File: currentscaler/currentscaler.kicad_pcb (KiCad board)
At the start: 2 copper layers, 76.1 x 33.4 mm, 27 parts, among them CON1 RS677-8759, CON2 RS677-8759, U1 LMV321, U2 MAX4239AUT, U3 MAX4239AUT

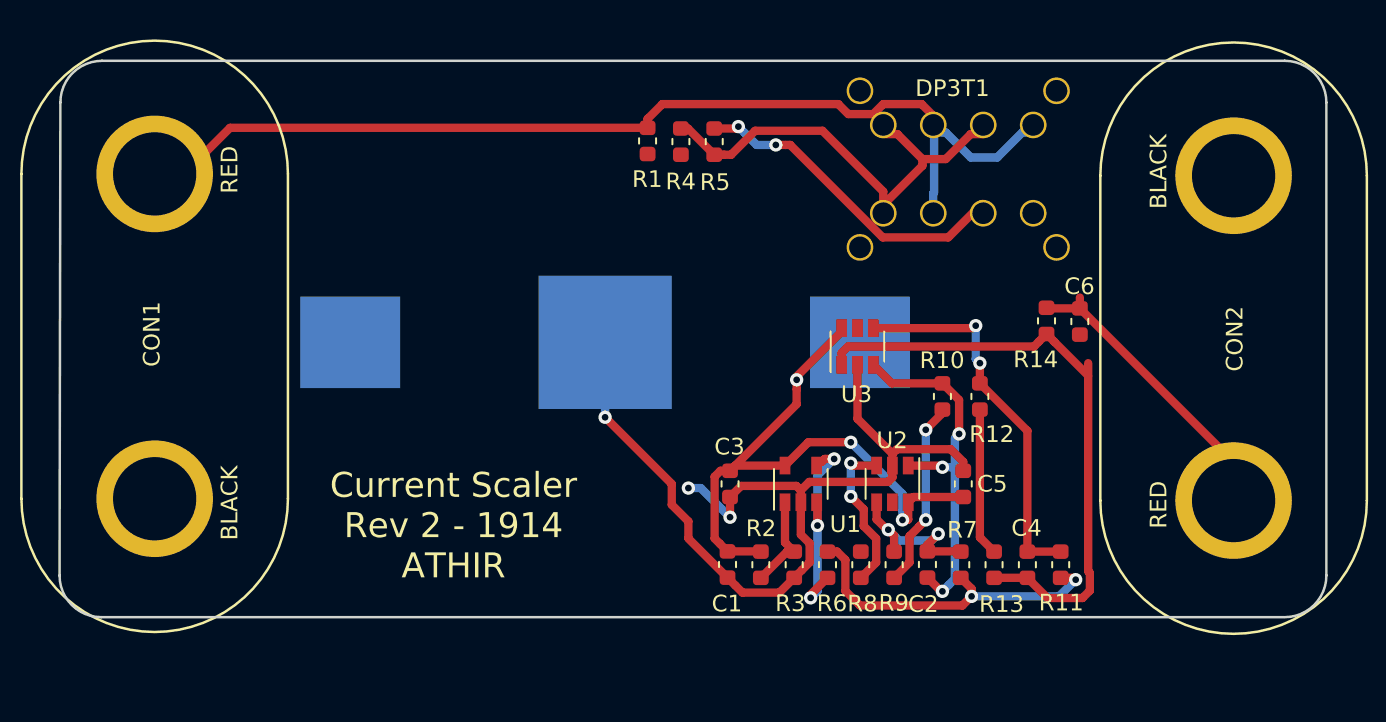
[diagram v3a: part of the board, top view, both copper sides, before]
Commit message: WIP: HW4
100 ohm resistors now 0805.
Fixed footprint of switch.
Removed 3V CR2450 holder.
Added silkscreen explanations.
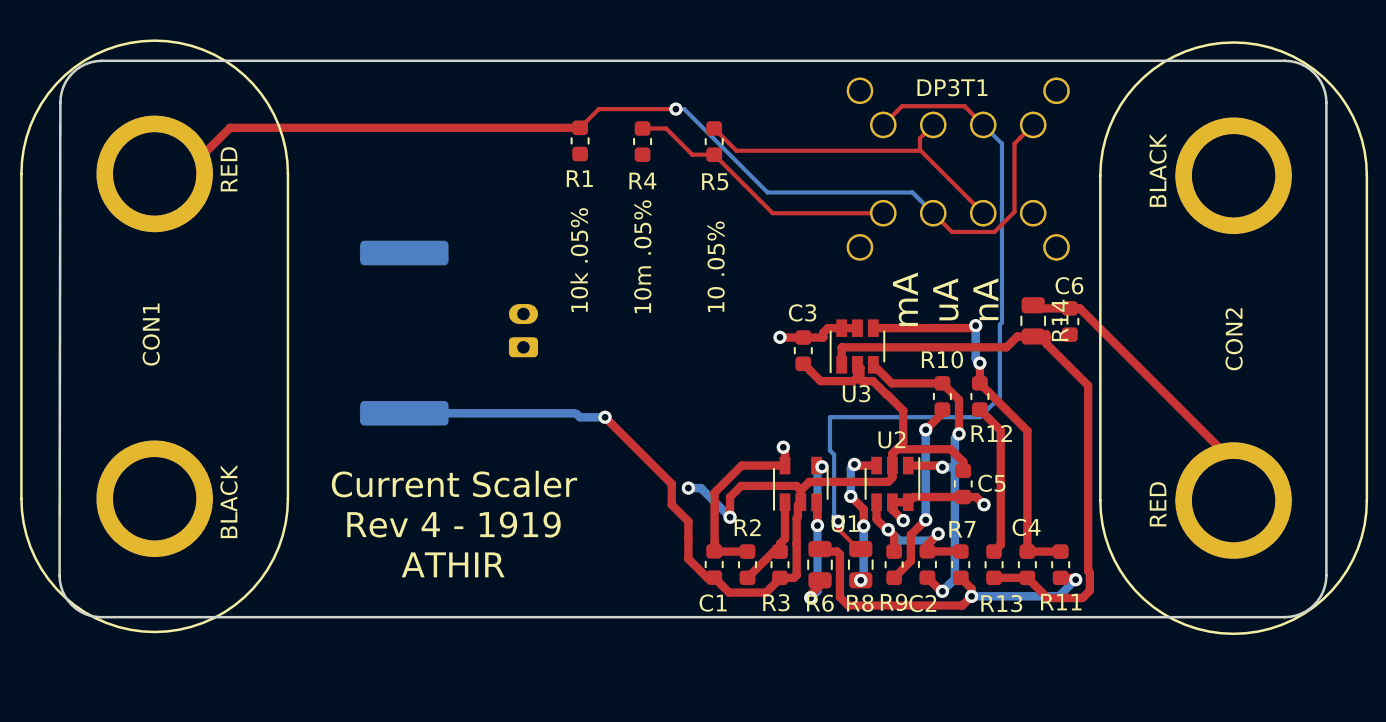
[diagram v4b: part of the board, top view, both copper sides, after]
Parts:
- added REF**: JST_PH_B2B-PH-K_1x02_P2.00mm_Vertical, Connector_JST:JST_PH_B2B-PH-K_1x02_P2.00mm_Vertical, B.Cu at (125.6, 109.8)
- BT1: footprint Battery:BatteryHolder_Keystone_3008_1x2450 -> Resistor_SMD:R_4020_10251Metric
- R14, R6, R8: footprint Resistor_SMD:R_0603_1608Metric -> Resistor_SMD:R_0805_2012Metric
- moved BT1 12.1 mm to (118.5, 109.0), turned to 270 degrees
- moved C3 9.13 mm to (142.4, 110.0)
- moved R1 4.05 mm to (129.0, 97.4)
- moved R4 2.30 mm to (132.8, 97.5)
- moved R3 0.85 mm to (141.0, 122.8)
- moved R14 0.80 mm to (156.2, 108.2)
- moved C1 0.80 mm to (137.1, 122.8)
- moved R2 0.80 mm to (139.1, 122.8)
- moved C6 0.60 mm to (158.4, 108.2)
- moved R6 0.45 mm to (143.4, 122.8)
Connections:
- BT1 pad 1: +9V -> +5V
- C1 pad 1: +9V -> +5V
- C3 pad 1: +9V -> +5V
- C5 pad 1: +9V -> +5V
- R2 pad 1: +9V -> +5V
- U1 pad 5: +9V -> +5V
- U2 pad 5: Net-(U2-Pad5) -> +5V
- U2 pad 6: +9V -> +5V
- U3 pad 5: Net-(U3-Pad5) -> +5V
- U3 pad 6: +9V -> +5V
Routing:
- net Net-(DP3T1-Pad6): track 0.00 -> 43.3 mm, vias 0 -> 1
- net +9V: track 37.9 -> 0.00 mm, vias 3 -> 0
- net +5V: track 0.00 -> 23.8 mm, vias 0 -> 4
- net GND: track 55.5 -> 70.4 mm
- net Net-(DP3T1-Pad4): track 26.6 -> 16.6 mm
- net Net-(R6-Pad2): track 13.2 -> 11.6 mm
- net Net-(R8-Pad1): track 9.51 -> 8.80 mm, vias 2 -> 4
- net Net-(C4-Pad1): track 37.2 -> 36.5 mm
- net Net-(CON1-Pad1): track 61.6 -> 61.3 mm, vias 0 -> 1
- net Net-(DP3T1-Pad2): track 20.0 -> 20.2 mm, vias 2 -> 0
- added copper zone on B.Cu, net +5V
- removed copper zone on B.Cu, net +9V
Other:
- outline, holes or cut-outs redrawn
- board text added: "5V"
- board text added: "Current Scaler Rev 4 - 1919 ATHIR"
- board text added: "GND"
- board text added: "mA uA nA"
- board text removed: "Current Scaler Rev 2 - 1914 ATHIR"

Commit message: HW 4 - commit
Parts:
- added C7: 100nF, Capacitor_SMD:C_0603_1608Metric, F.Cu at (141.8, 113.6)
- added U4: MAX44246, athir:uMAX8, F.Cu at (135.9, 112.8)
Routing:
- net Net-(C2-Pad2): track 10.2 -> 30.2 mm, vias 2 -> 3
- net Net-(C2-Pad1): track 22.2 -> 39.5 mm, vias 3 -> 5
- net Net-(C4-Pad2): track 23.1 -> 36.9 mm, vias 2 -> 4
- net Net-(R8-Pad1): track 8.80 -> 22.4 mm
- net Net-(C4-Pad1): track 36.5 -> 47.3 mm
- net GND: track 70.4 -> 75.8 mm
- net Net-(C7-Pad2): track 0.00 -> 3.92 mm
- net +5V: track 23.8 -> 23.3 mm
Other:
- board text added: "Current Scaler Rev 4 - 1922 ATHIR"
- board text removed: "Current Scaler Rev 4 - 1919 ATHIR"

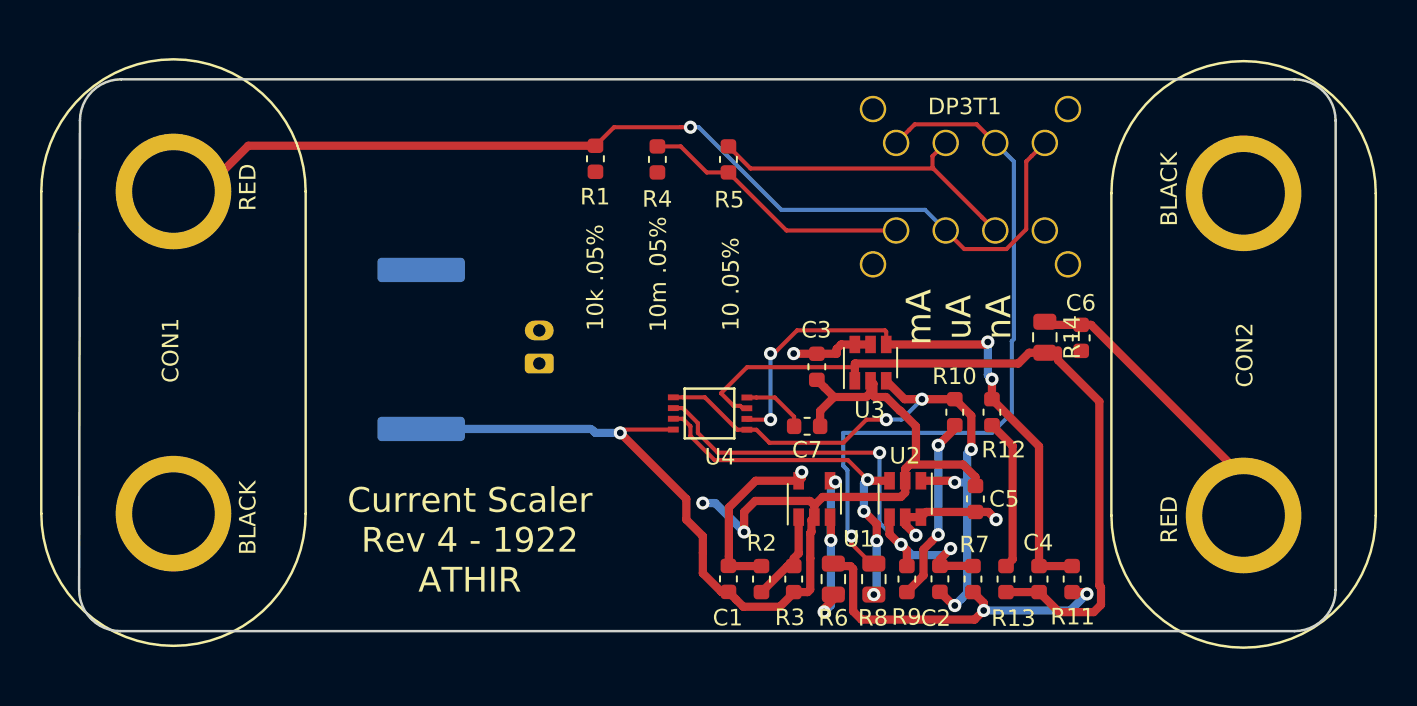
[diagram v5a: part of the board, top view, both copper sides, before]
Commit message: Rev 5 1936
Fixed 5V missing on opamp. 
Added duplicate power and resistor pairs.
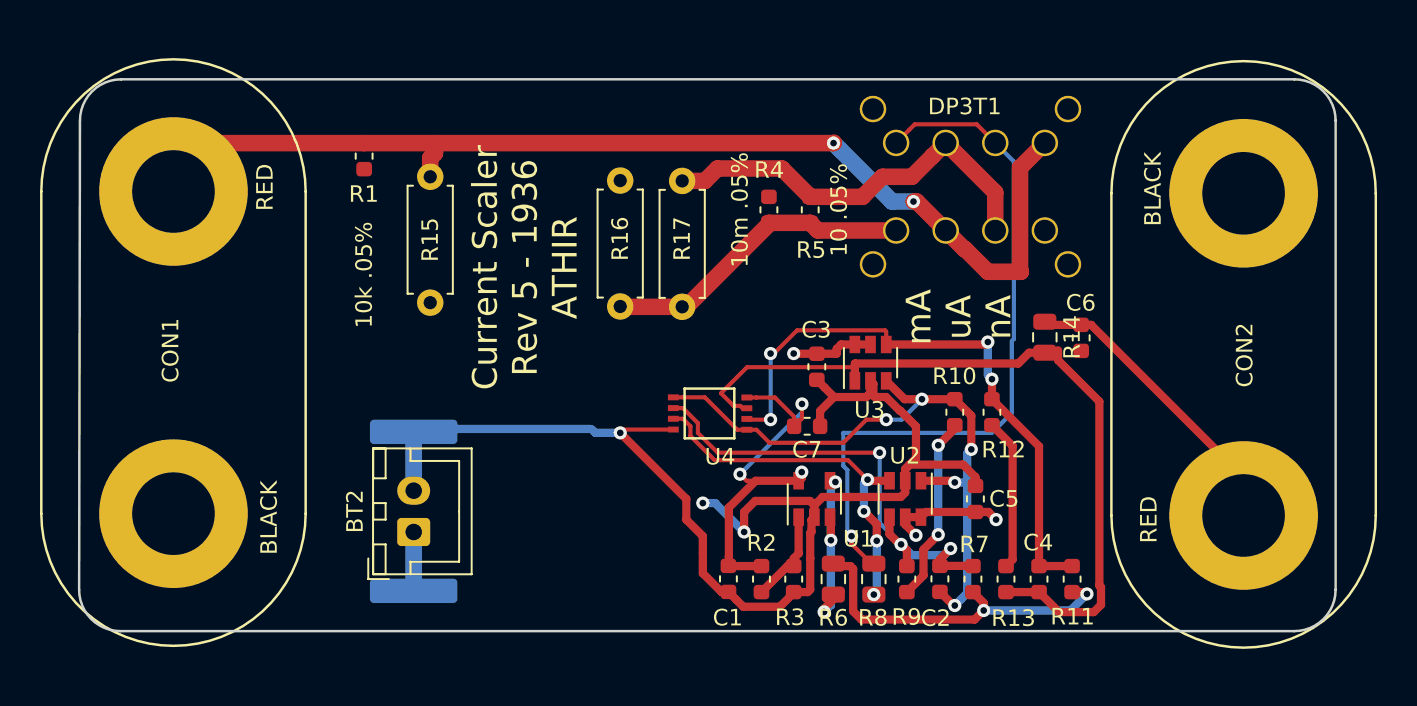
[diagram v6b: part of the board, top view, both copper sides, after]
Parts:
- removed REF**: JST_PH_B2B-PH-K_1x02_P2.00mm_Vertical, Connector_JST:JST_PH_B2B-PH-K_1x02_P2.00mm_Vertical
- added BT2: Battery_Cell, Connector_JST:JST_XH_B2B-XH-A_1x02_P2.50mm_Vertical, F.Cu at (118.0, 120.0)
- added R15: 10k .05%, Resistor_THT:R_Axial_DIN0207_L6.3mm_D2.5mm_P7.62mm_Horizontal, F.Cu at (119.0, 98.5)
- added R16: 10m .05%, Resistor_THT:R_Axial_DIN0207_L6.3mm_D2.5mm_P7.62mm_Horizontal, F.Cu at (130.5, 106.3)
- added R17: 10 .05%, Resistor_THT:R_Axial_DIN0207_L6.3mm_D2.5mm_P7.62mm_Horizontal, F.Cu at (134.2, 98.8)
- R14, R6, R8: value 100 -> 220
- moved R1 14.0 mm to (115.0, 97.2)
- moved BT1 9.81 mm to (118.0, 118.8), turned to 90 degrees
- moved R4 7.41 mm to (139.5, 100.5), turned to 90 degrees
- moved R5 5.81 mm to (142.0, 100.5)
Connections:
- C7 pad 2: Net-(C7-Pad2) -> +5V
- DP3T1 pad 1: Net-(DP3T1-Pad1) -> (no net)
- U4 pad 8: Net-(C7-Pad2) -> +5V
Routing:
- net +5V: track 23.3 -> 39.2 mm, vias 4 -> 6
- net Net-(CON1-Pad1): track 61.3 -> 66.4 mm, vias 1 -> 2
- net Net-(DP3T1-Pad2): track 20.2 -> 24.6 mm
- net Net-(C7-Pad2): track 3.92 -> 0.00 mm
- net GND: track 75.8 -> 79.3 mm
- net Net-(DP3T1-Pad4): track 16.6 -> 18.8 mm
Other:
- board text added: "Current Scaler Rev 5 - 1936 ATHIR"
- board text removed: "Current Scaler Rev 4 - 1922 ATHIR"
